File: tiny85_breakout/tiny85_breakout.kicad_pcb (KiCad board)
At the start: 2 copper layers, 20.3 x 15.9 mm, 4 parts, among them J1 Conn_01x04_Male, J2 Conn_01x04_Male, U1 ATTINY85-20PU

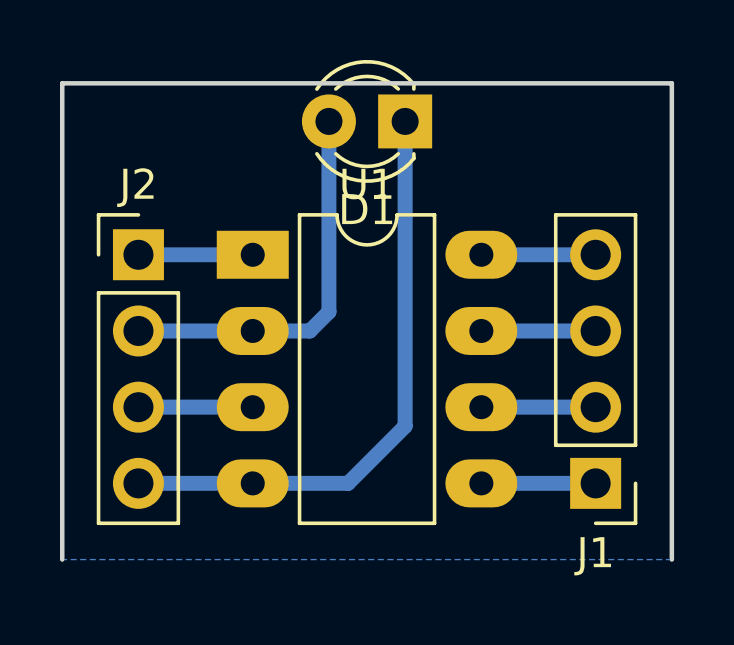
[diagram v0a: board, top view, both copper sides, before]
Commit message: updated ocb to NOT use copper fill in kicad. This makes better geometry in flatcam!
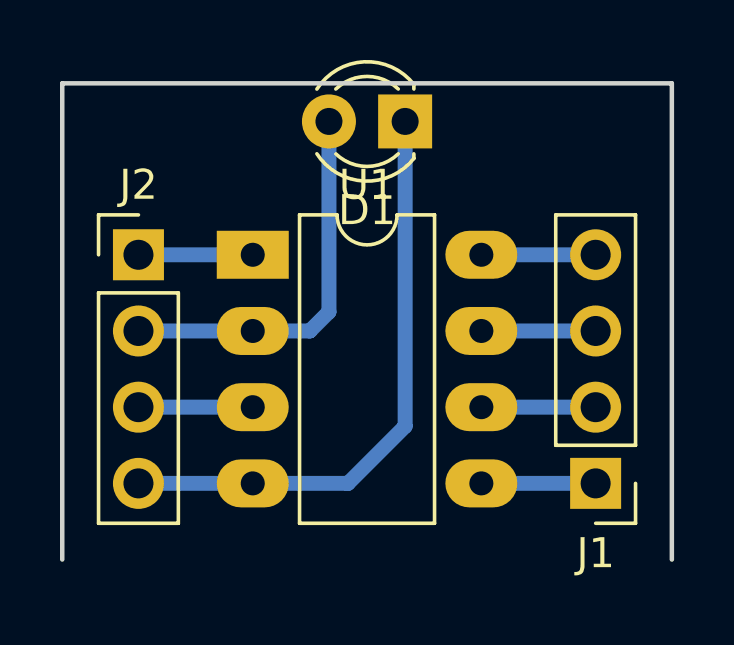
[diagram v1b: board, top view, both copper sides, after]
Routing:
- removed copper zone on B.Cu, net (none)
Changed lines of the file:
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@@
   (gr_line (start 142.24 99.695) (end 162.56 99.695) (angle 90) (layer Edge.Cuts) (width 0.15))
   (gr_line (start 142.24 115.57) (end 142.24 99.695) (angle 90) (layer Edge.Cuts) (width 0.15))
-  (segment (start 144.78 113.03) (end 148.59 113.03) (width 0.5) (layer B.Cu) (net 1) (status C00000))
-  (segment (start 148.59 113.03) (end 151.765 113.03) (width 0.5) (layer B.Cu) (net 1) (status 400000))
+  (segment (start 144.78 113.03) (end 148.59 113.03) (width 0.5) (layer B.Cu) (net 1))
+  (segment (start 148.59 113.03) (end 151.765 113.03) (width 0.5) (layer B.Cu) (net 1))
   (segment (start 151.765 113.03) (end 153.67 111.125) (width 0.5) (layer B.Cu) (net 1))
-  (segment (start 153.67 111.125) (end 153.67 100.965) (width 0.5) (layer B.Cu) (net 1) (status 800000))
+  (segment (start 153.67 111.125) (end 153.67 100.965) (width 0.5) (layer B.Cu) (net 1))
   (segment (start 144.78 107.95) (end 148.59 107.95) (width 0.5) (layer B.Cu) (net 2))
   (segment (start 148.59 107.95) (end 150.495 107.95) (width 0.5) (layer B.Cu) (net 2))
   (segment (start 150.495 107.95) (end 151.13 107.315) (width 0.5) (layer B.Cu) (net 2))
   (segment (start 151.13 107.315) (end 151.13 100.965) (width 0.5) (layer B.Cu) (net 2))
-  (segment (start 156.21 113.03) (end 160.02 113.03) (width 0.5) (layer B.Cu) (net 3) (status C00000))
-  (segment (start 156.21 110.49) (end 160.02 110.49) (width 0.5) (layer B.Cu) (net 4) (status C00000))
-  (segment (start 156.21 107.95) (end 160.02 107.95) (width 0.5) (layer B.Cu) (net 5) (status C00000))
-  (segment (start 156.21 105.41) (end 160.02 105.41) (width 0.5) (layer B.Cu) (net 6) (status C00000))
-  (segment (start 144.78 105.41) (end 148.59 105.41) (width 0.5) (layer B.Cu) (net 7) (status C00000))
-  (segment (start 144.78 110.49) (end 148.59 110.49) (width 0.5) (layer B.Cu) (net 8) (status C00000))
-  (zone (net 0) (net_name "") (layer B.Cu) (hatch edge 0.508)
-    (connect_pads (clearance 0.15))
-    (min_thickness 0.254)
-    (fill yes (arc_segments 16) (thermal_gap 0.508) (thermal_bridge_width 0.508))
-    (polygon
-      (pts
-        (xy 162.56 115.57) (xy 142.24 115.57) (xy 142.24 99.695) (xy 162.56 99.695) (xy 162.56 115.57)
-      )
-    )
-  )
+  (segment (start 156.21 113.03) (end 160.02 113.03) (width 0.5) (layer B.Cu) (net 3))
+  (segment (start 156.21 110.49) (end 160.02 110.49) (width 0.5) (layer B.Cu) (net 4))
+  (segment (start 156.21 107.95) (end 160.02 107.95) (width 0.5) (layer B.Cu) (net 5))
+  (segment (start 156.21 105.41) (end 160.02 105.41) (width 0.5) (layer B.Cu) (net 6))
+  (segment (start 144.78 105.41) (end 148.59 105.41) (width 0.5) (layer B.Cu) (net 7))
+  (segment (start 144.78 110.49) (end 148.59 110.49) (width 0.5) (layer B.Cu) (net 8))
 )
